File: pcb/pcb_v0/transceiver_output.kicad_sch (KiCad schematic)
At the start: 23 parts, among them J1 Conn_02x04_Odd_Even, U1 MAX3221EIPWR

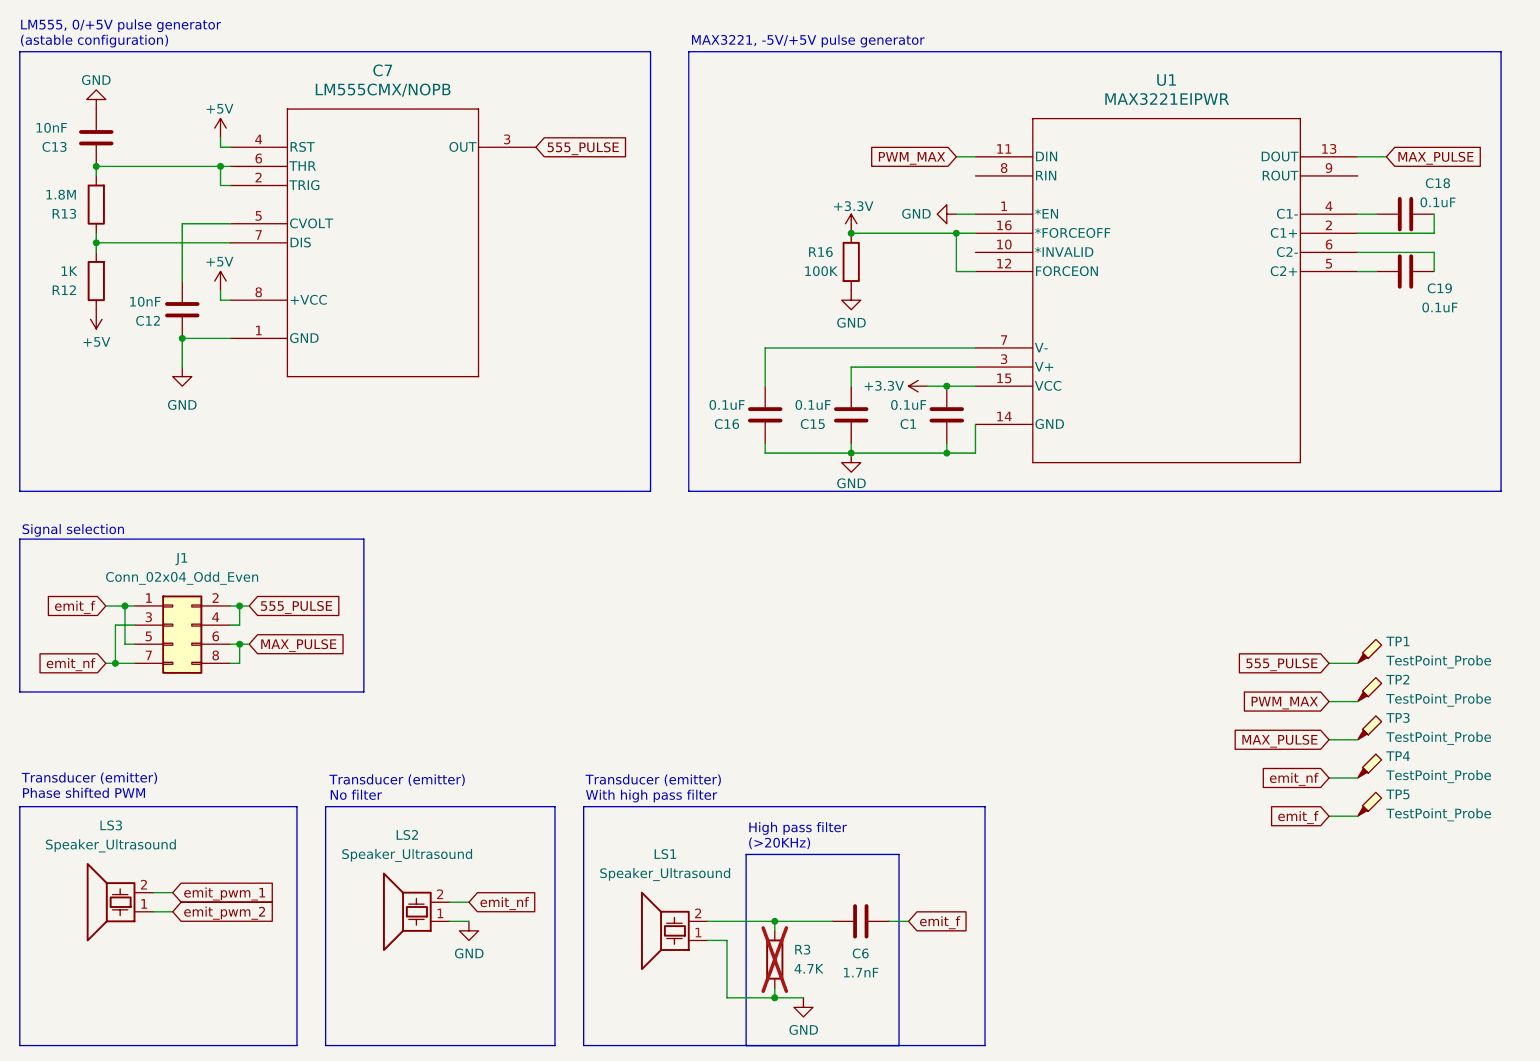
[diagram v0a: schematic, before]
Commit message: fix(pcb_v0): Update resistor and capacitor values
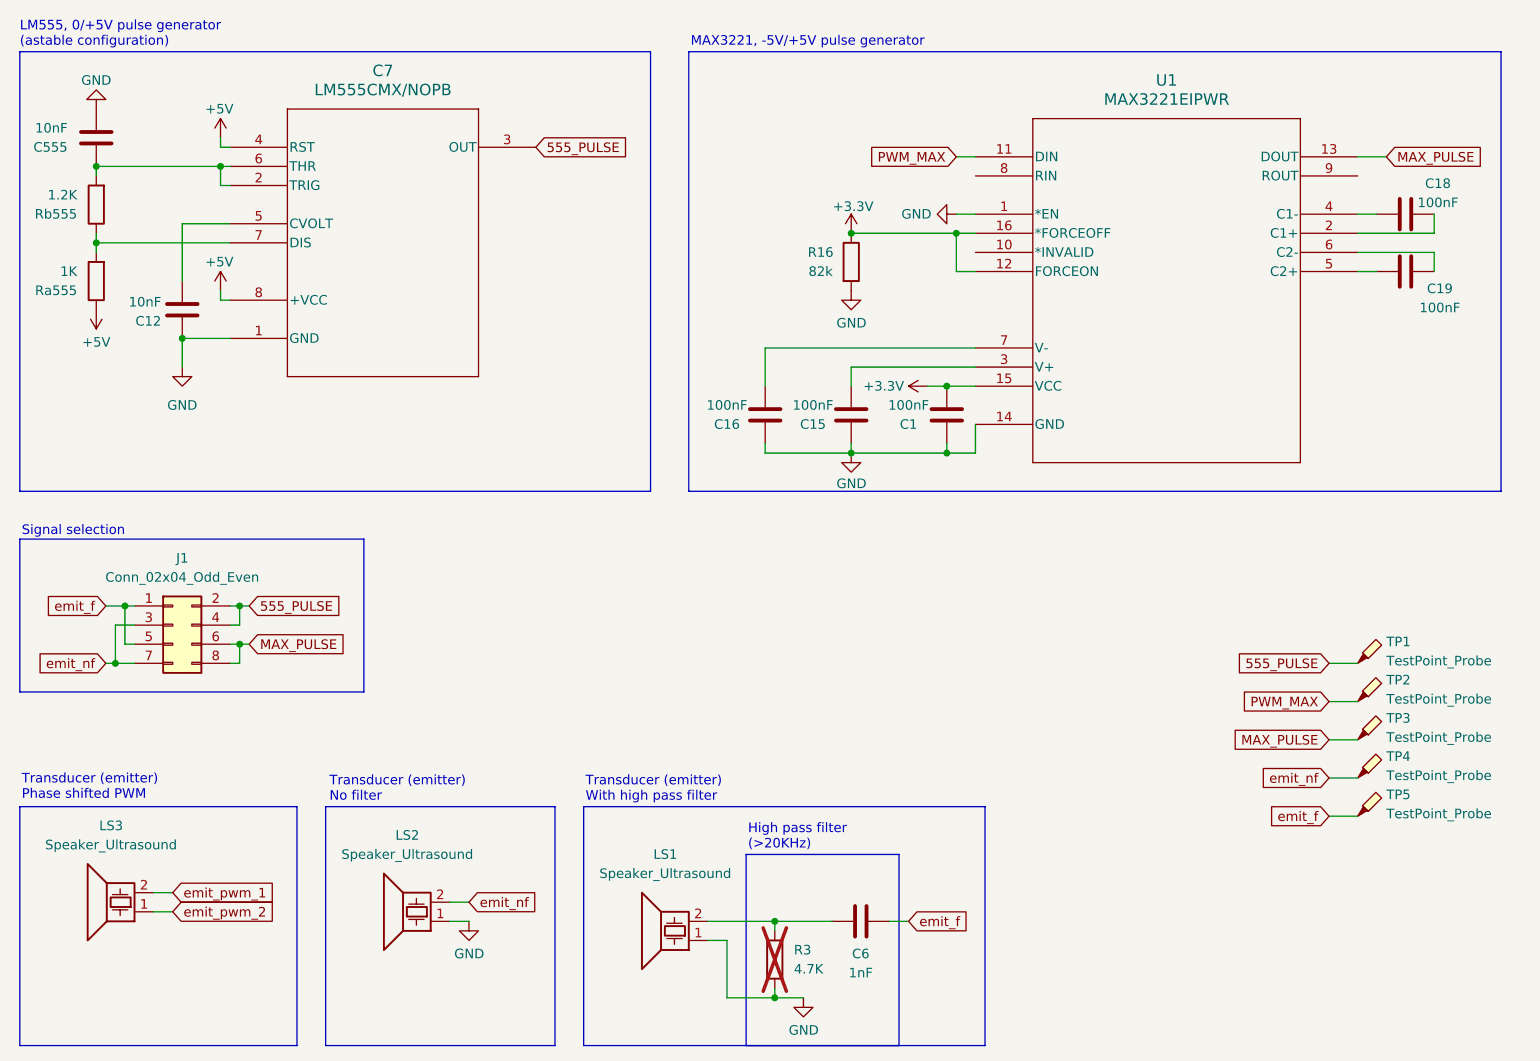
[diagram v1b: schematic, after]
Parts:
- C1, C15, C16, C18, C19: value 0.1uF -> 100nF
- C555: renamed from C13; footprint Capacitor_THT:C_Disc_D4.3mm_W1.9mm_P5.00mm -> (none)
- C6: value 1.7nF -> 1nF
- R16: value 100K -> 82k
- Rb555: renamed from R13; value 1.8M -> 1.2K
- renumbered R12 to Ra555
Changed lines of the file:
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@@
 			)
 		)
-		(property "Value" "0.1uF"
+		(property "Value" "100nF"
 			(at 116.84 72.39 0)
 			(effects
@@
 		(dnp no)
 		(fields_autoplaced yes)
-		(property "Reference" "R13"
+		(property "Reference" "Rb555"
 			(at 30.48 46.9901 0)
 			(effects
@@
 			)
 		)
-		(property "Value" "1.8M"
+		(property "Value" "1.2K"
 			(at 30.48 44.4501 0)
 			(effects
@@
 			(project "pcb_v0"
 				(path "/a4ba1476-565f-4ee3-b0bb-c20cd60fbb7a/eb101bc7-4324-4c12-9718-71e0561db175"
-					(reference "R13")
+					(reference "Rb555")
 					(unit 1)
 				)
@@
 		(on_board yes)
 		(dnp no)
-		(property "Reference" "C13"
+		(property "Reference" "C555"
 			(at 29.21 38.1001 0)
 			(effects
@@
 			)
 		)
-		(property "Footprint" "Capacitor_THT:C_Disc_D4.3mm_W1.9mm_P5.00mm"
+		(property "Footprint" ""
 			(at 32.0548 33.02 0)
 			(effects
@@
 			(project "pcb_v0"
 				(path "/a4ba1476-565f-4ee3-b0bb-c20cd60fbb7a/eb101bc7-4324-4c12-9718-71e0561db175"
-					(reference "C13")
+					(reference "C555")
 					(unit 1)
 				)
@@
 			)
 		)
-		(property "Value" "0.1uF"
+		(property "Value" "100nF"
 			(at 128.27 72.39 0)
 			(effects
@@
 			)
 		)
-		(property "Value" "0.1uF"
+		(property "Value" "100nF"
 			(at 211.582 59.436 90)
 			(effects
@@
 			)
 		)
-		(property "Value" "0.1uF"
+		(property "Value" "100nF"
 			(at 211.328 45.466 90)
 			(effects
@@
 			)
 		)
-		(property "Value" "100K"
+		(property "Value" "82k"
 			(at 129.286 54.61 0)
 			(effects
@@
 		(dnp no)
 		(fields_autoplaced yes)
-		(property "Reference" "R12"
+		(property "Reference" "Ra555"
 			(at 30.48 57.1501 0)
 			(effects
@@
 			(project "pcb_v0"
 				(path "/a4ba1476-565f-4ee3-b0bb-c20cd60fbb7a/eb101bc7-4324-4c12-9718-71e0561db175"
-					(reference "R12")
+					(reference "Ra555")
 					(unit 1)
 				)
@@
 			)
 		)
-		(property "Value" "0.1uF"
+		(property "Value" "100nF"
 			(at 140.97 72.39 0)
 			(effects
@@
 			)
 		)
-		(property "Value" "1.7nF"
+		(property "Value" "1nF"
 			(at 134.62 147.828 90)
 			(effects
